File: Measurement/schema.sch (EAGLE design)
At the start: 8 parts

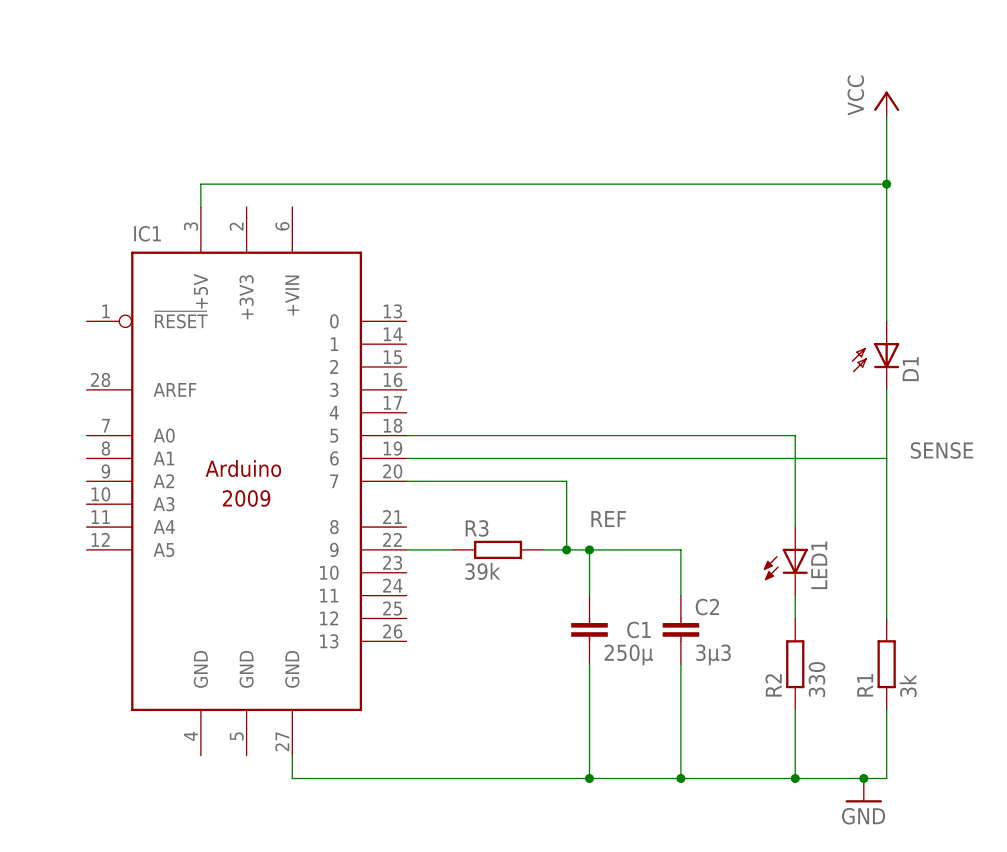
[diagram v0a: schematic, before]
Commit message: Update schema with analog measurement
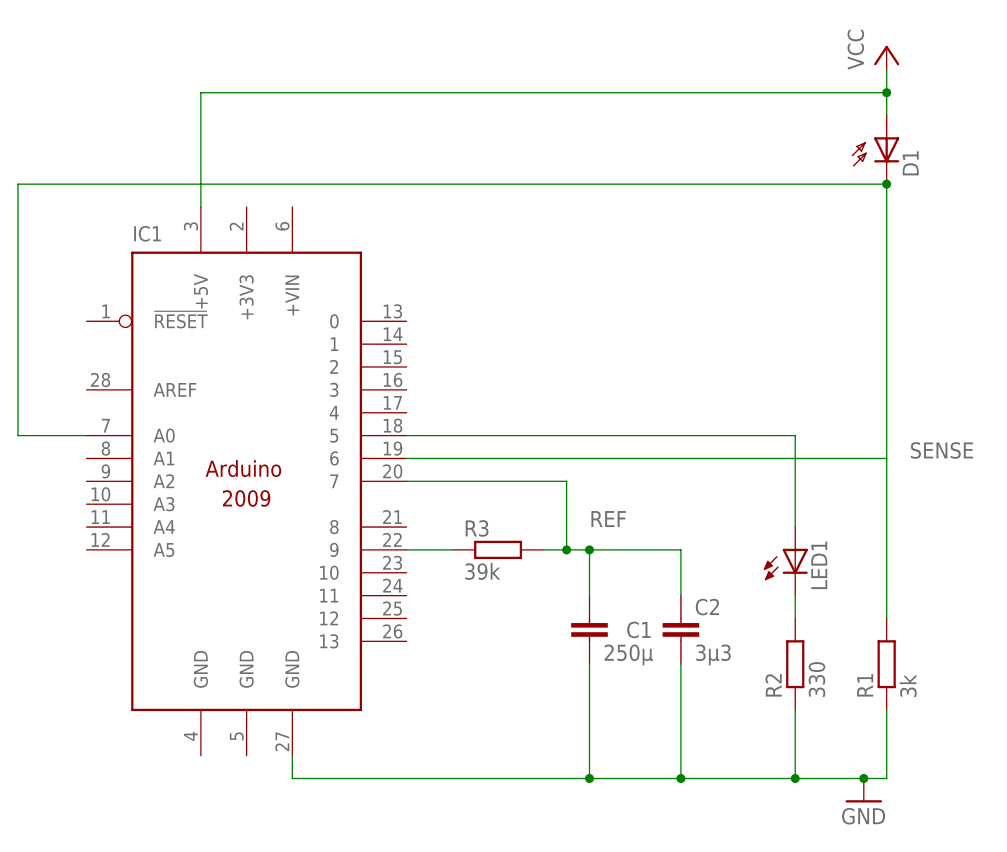
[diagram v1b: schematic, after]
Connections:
- net SENSE: now also IC1.A0
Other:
- moved on the sheet: D1
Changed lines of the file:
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@@
 <attribute name="NAME" x="27.94" y="67.31" size="1.6764" layer="95"/>
 </instance>
-<instance part="D1" gate="1" x="111.76" y="55.88">
-<attribute name="NAME" x="115.316" y="51.562" size="1.778" layer="95" rot="R90"/>
-<attribute name="VALUE" x="117.475" y="51.562" size="1.778" layer="96" rot="R90" display="off"/>
+<instance part="D1" gate="1" x="111.76" y="78.74">
+<attribute name="NAME" x="115.316" y="74.422" size="1.778" layer="95" rot="R90"/>
+<attribute name="VALUE" x="117.475" y="74.422" size="1.778" layer="96" rot="R90" display="off"/>
 </instance>
 <instance part="LED1" gate="G$1" x="101.6" y="33.02">
@@
 <attribute name="VALUE" x="106.68" y="2.54" size="1.778" layer="96"/>
 </instance>
-<instance part="P+1" gate="VCC" x="111.76" y="83.82">
-<attribute name="VALUE" x="109.22" y="81.28" size="1.778" layer="96" rot="R90"/>
+<instance part="P+1" gate="VCC" x="111.76" y="88.9">
+<attribute name="VALUE" x="109.22" y="86.36" size="1.778" layer="96" rot="R90"/>
 </instance>
 <instance part="C2" gate="G$1" x="88.9" y="25.4">
@@
 <pinref part="D1" gate="1" pin="C"/>
 <pinref part="IC1" gate="G$1" pin="6"/>
-<wire x1="111.76" y1="50.8" x2="111.76" y2="43.18" width="0.1524" layer="91"/>
+<wire x1="111.76" y1="73.66" x2="111.76" y2="43.18" width="0.1524" layer="91"/>
 <wire x1="111.76" y1="43.18" x2="58.42" y2="43.18" width="0.1524" layer="91"/>
 <pinref part="R1" gate="G$1" pin="2"/>
 <wire x1="111.76" y1="25.4" x2="111.76" y2="43.18" width="0.1524" layer="91"/>
 <label x="114.3" y="43.18" size="1.778" layer="95"/>
+<pinref part="IC1" gate="G$1" pin="A0"/>
+<wire x1="15.24" y1="73.66" x2="111.76" y2="73.66" width="0.1524" layer="91"/>
+<junction x="111.76" y="73.66"/>
+<wire x1="22.86" y1="45.72" x2="15.24" y2="45.72" width="0.1524" layer="91"/>
+<wire x1="15.24" y1="45.72" x2="15.24" y2="73.66" width="0.1524" layer="91"/>
 </segment>
 </net>
@@
 <pinref part="P+1" gate="VCC" pin="VCC"/>
 <pinref part="D1" gate="1" pin="A"/>
-<wire x1="111.76" y1="81.28" x2="111.76" y2="73.66" width="0.1524" layer="91"/>
+<wire x1="111.76" y1="86.36" x2="111.76" y2="83.82" width="0.1524" layer="91"/>
 <pinref part="IC1" gate="G$1" pin="+5V"/>
-<wire x1="111.76" y1="73.66" x2="111.76" y2="58.42" width="0.1524" layer="91"/>
-<wire x1="35.56" y1="71.12" x2="35.56" y2="73.66" width="0.1524" layer="91"/>
-<wire x1="35.56" y1="73.66" x2="111.76" y2="73.66" width="0.1524" layer="91"/>
-<junction x="111.76" y="73.66"/>
+<wire x1="111.76" y1="83.82" x2="111.76" y2="81.28" width="0.1524" layer="91"/>
+<wire x1="35.56" y1="71.12" x2="35.56" y2="83.82" width="0.1524" layer="91"/>
+<wire x1="35.56" y1="83.82" x2="111.76" y2="83.82" width="0.1524" layer="91"/>
+<junction x="111.76" y="83.82"/>
 </segment>
 </net>
